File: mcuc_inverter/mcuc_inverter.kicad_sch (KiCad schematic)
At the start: 0 parts

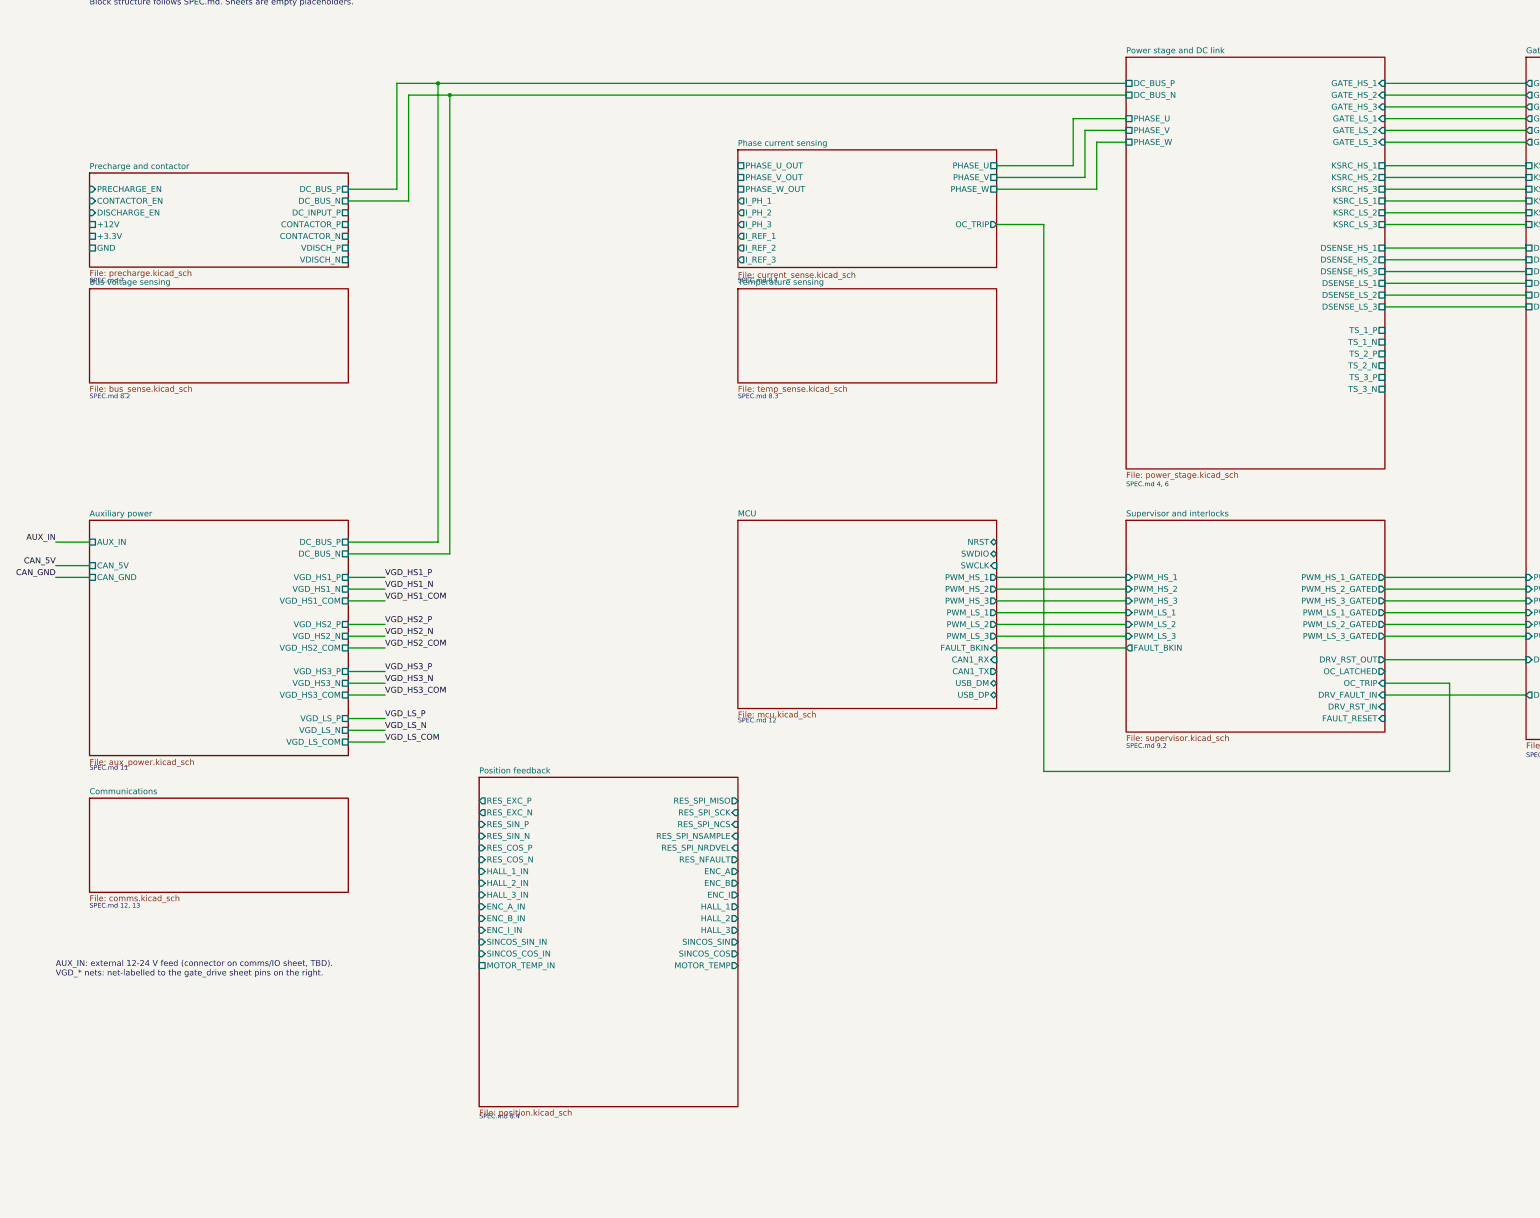
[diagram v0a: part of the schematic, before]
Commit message: Capture bus_sense, temp_sense, comms: all 11 sheets now live
bus_sense: 4x750k + 12.0k string (strict series, 124.5 V/part) into
AMC1311BDWV (pinout verified vs SBAS786C; B-grade 3.0-5.5 V VDD1 is
load-bearing per D022; no input clamp diodes per TI 9.3), HV-side
3.3 V from MCP1804T-3302 (2-28 V in, stocked - no TBV needed) off
the VGD_LS rail, diff-to-SE gain 0.75: V_BUS = 2.988 mV/V, 500 V ->
1.494 V, saturates ~1.50 V, always < 3.3 V.

temp_sense: coldplate NTC channel (B57861S off-board via J1101),
board NTC (NCU18 successor), 6x DNP TS provision pads onto the
module TS pins with D022 rationale quoted on-sheet.

comms: ISO1042DWR isolated CAN (VCC2 pins 11/16 tied - datasheet
requirement), split termination + TVS added (legacy sheet flagged
its own missing protection), USB-C + USBLC6 to MCU 70/71, keyed SWD,
status LEDs, I/O connectors. CAN_TX/RX verified onto MCU pins 96/95;
CONTACTOR_P/N resolve onto the precharge coil driver.

ERC 0 errors; netlist machine-checks per sheet; key cross-sheet
nets independently re-verified. 11 of 11 sheets captured.

Co-Authored-By: Claude Fable 5 <noreply@anthropic.com>
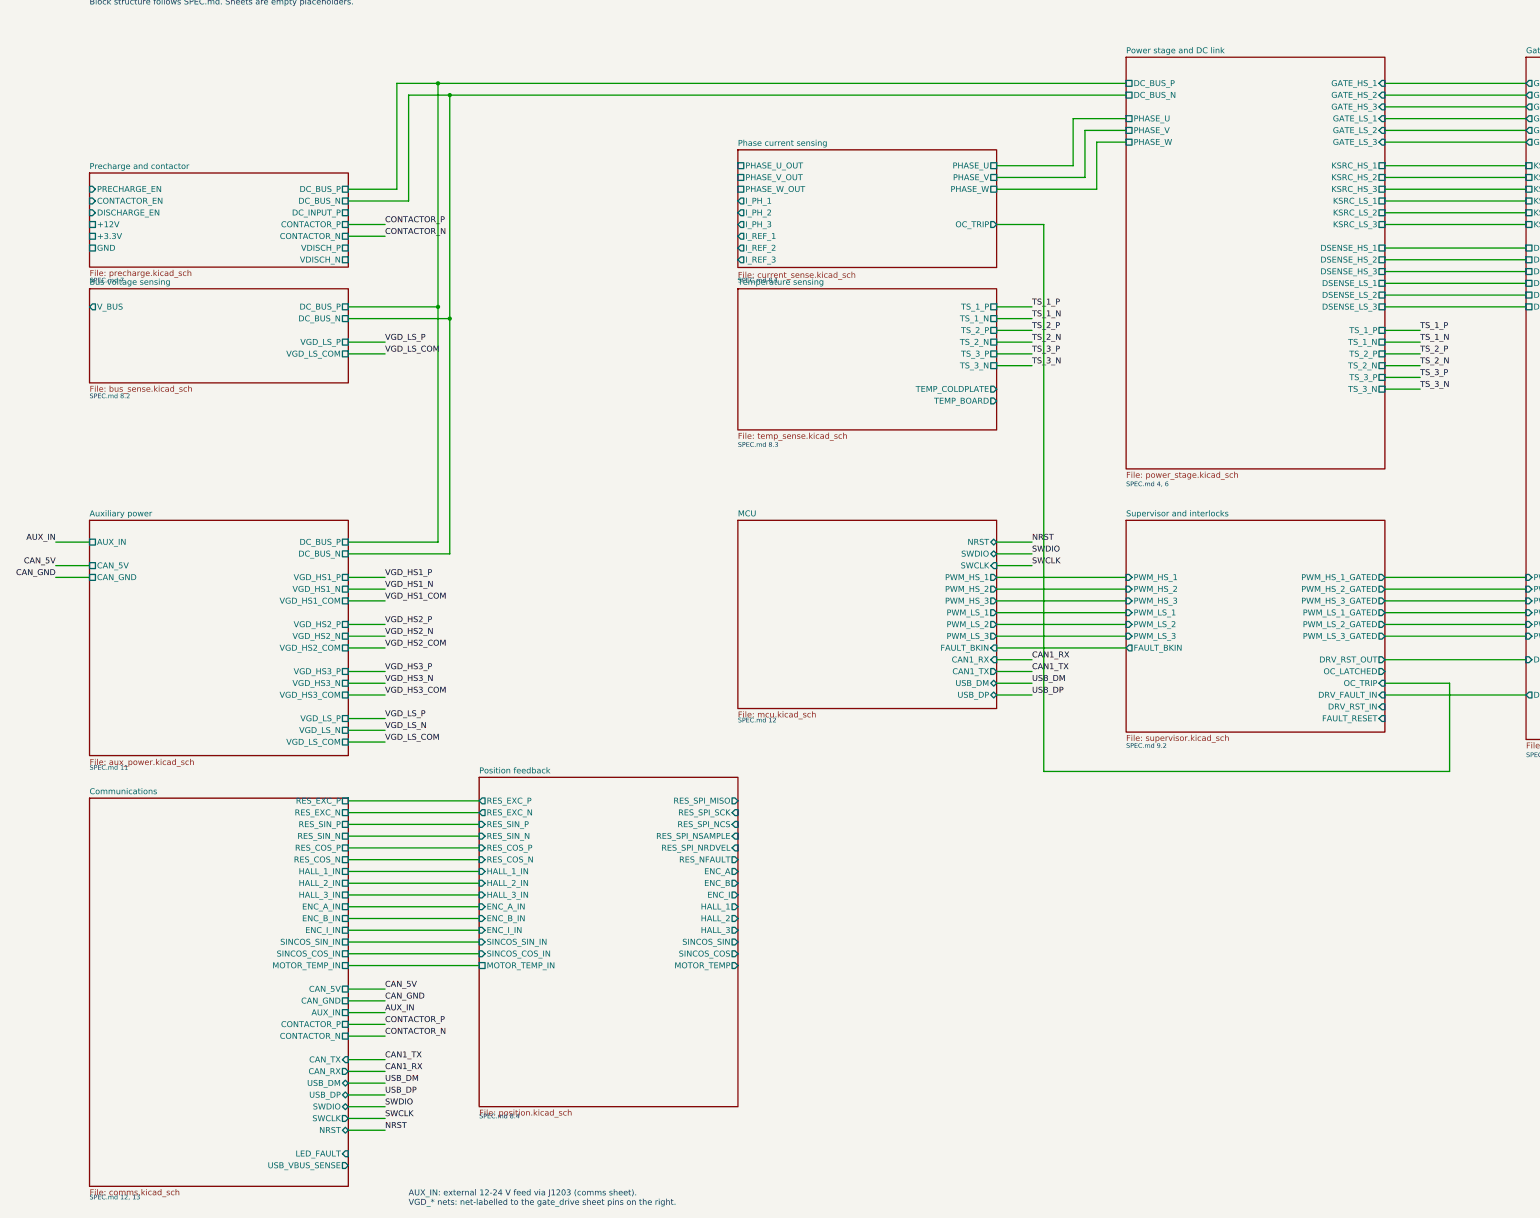
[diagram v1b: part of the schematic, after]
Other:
- sheet Bus voltage sensing ports: added DC_BUS_N, DC_BUS_P, VGD_LS_COM, VGD_LS_P, V_BUS; removed none
- sheet Communications ports: added AUX_IN, CAN_5V, CAN_GND, CAN_RX, CAN_TX, CONTACTOR_N, CONTACTOR_P, ENC_A_IN, ENC_B_IN, ENC_I_IN, HALL_1_IN, HALL_2_IN, HALL_3_IN, LED_FAULT, MOTOR_TEMP_IN, NRST, RES_COS_N, RES_COS_P, RES_EXC_N, RES_EXC_P, RES_SIN_N, RES_SIN_P, SINCOS_COS_IN, SINCOS_SIN_IN, SWCLK, SWDIO, USB_DM, USB_DP, USB_VBUS_SENSE; removed none
- sheet Temperature sensing ports: added TEMP_BOARD, TEMP_COLDPLATE, TS_1_N, TS_1_P, TS_2_N, TS_2_P, TS_3_N, TS_3_P; removed none
- note added: "AUX_IN: external 12-24 V feed via J1203 (comms sheet). VGD_* nets: net-labelled to the gate_drive sheet pins on the right."
- note removed: "AUX_IN: external 12-24 V feed (connector on comms/IO sheet, TBD). VGD_* nets: net-labelled to the gate_drive sheet pins on the right."

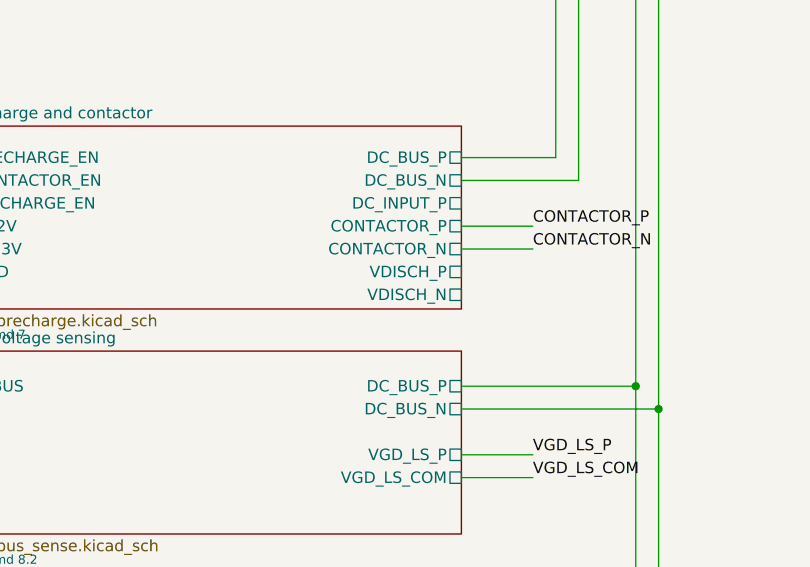
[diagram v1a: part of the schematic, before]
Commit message: Precharge: VOM1271T photovoltaic discharge drive; fix gate pulldown
Swap the active-discharge opto to VOM1271T (pinout verified from
Vishay 83469 Rev 1.9; SOP-4 symbol added to project lib) driven at
~19 mA from DISCHARGE_EN (R427 330R -> 100R). Deletes the
VDISCH_P/N floating-supply labels, flags and root pins entirely -
the photovoltaic driver needs no secondary supply and integrates
rapid gate turn-off.

Fix found during the swap: the 10k gate pulldown (R426) would have
clamped the VOM1271's 15-47 uA output to ~0.2 V - below the FET
threshold, discharge would never fire. Raised to 10M per the Vishay
test circuit; turn-off is handled by the driver's integrated
circuit, and the 10M still bleeds the gate if the driver is
unpopulated. Zener updated to stocked MM3Z18VT1G (D022 BOM sweep).

ERC 0 errors; netlist checks by the edit agent (LED loop, gate net,
DC_BUS_N membership, zero VDISCH nets remain).

Co-Authored-By: Claude Fable 5 <noreply@anthropic.com>
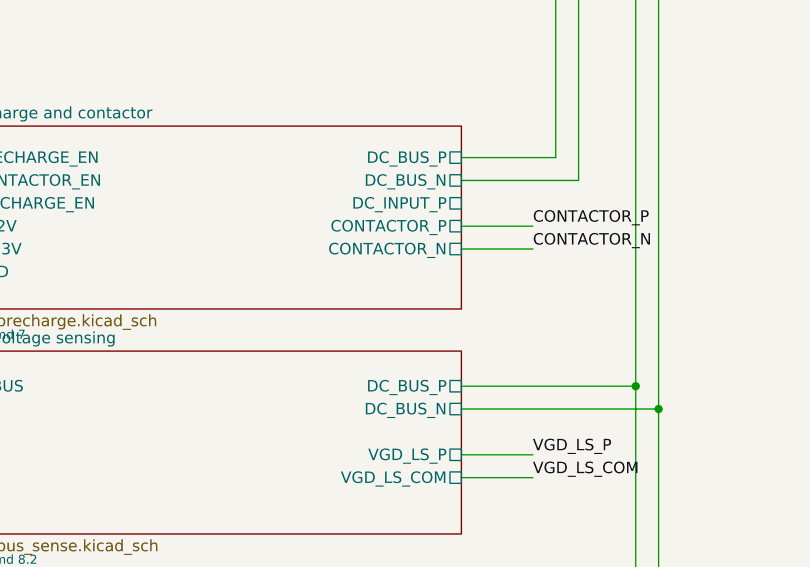
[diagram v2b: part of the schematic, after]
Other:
- sheet Precharge and contactor ports: added none; removed VDISCH_N, VDISCH_P
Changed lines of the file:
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@@
-			)
-		)
-		(pin "VDISCH_P" passive
-			(at 75.88 76.2 0)
-			(effects
-				(font
-					(size 1.27 1.27)
-				)
-				(justify right)
-			)
-		)
-		(pin "VDISCH_N" passive
-			(at 75.88 78.74 0)
-			(effects
-				(font
-					(size 1.27 1.27)
-				)
-				(justify right)
 			)
 		)

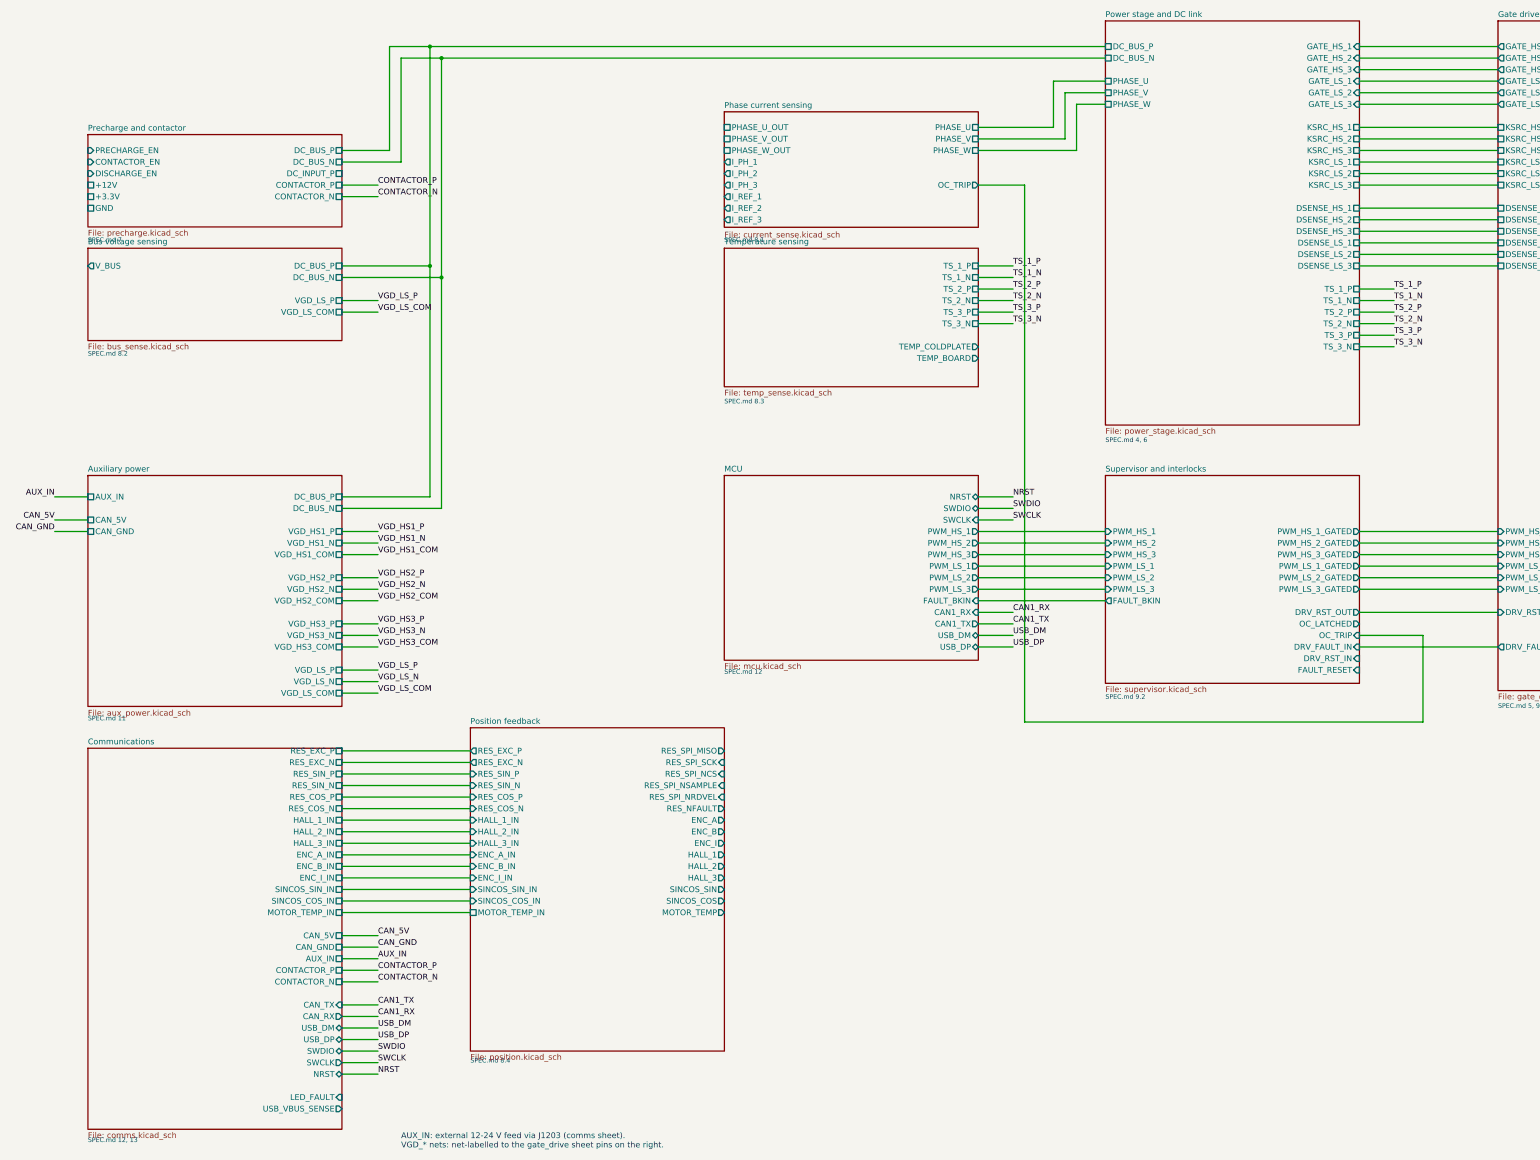
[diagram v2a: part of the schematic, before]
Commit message: Wire full MCU pin map; add verified PINOUT.md
All 33 remaining signals wired per the citation-verified map (D023):
phase currents PC0/1/2 on VESC triple-simultaneous ADC channels,
V_BUS PC3, temps PA3/PB0/PC4, SinCos PA5/PA6, I_REF PA4/PA7/PB1,
encoder PC6/7/8 (TIM3), halls PD12/13/14, resolver SPI3 PC10/PC11 +
PA15 boot-safe CS + PD0/PD1/PD2 controls, supervisor GPIOs PD3/4/5,
precharge/contactor/discharge PE2/3/4, LED PE0, VBUS sense PC5, PPM
PB6 (TIM4_CH1, VESC convention - repurposed J1206 spare pin).
PA0/1/2 and PB10/11 reserved with on-sheet notes.

AD2S1205 drive validated in-datasheet: VIH 2.0 V @ 5 V supply, so
3.3 V MCU outputs are legal; its 5 V outputs land on FT pins only.

docs/PINOUT.md: complete table with per-row DS8626 Table 7/9
citations, 5V-tolerance column with the analog-mode caveat, and the
D023 reservations - generated against the post-wiring netlist.

ERC 0 errors (warnings down 224 -> 201 as dangling pins connected).
33/33 nets machine-verified U1-pad-to-counterpart; 6 re-verified
independently before commit.

Co-Authored-By: Claude Fable 5 <noreply@anthropic.com>
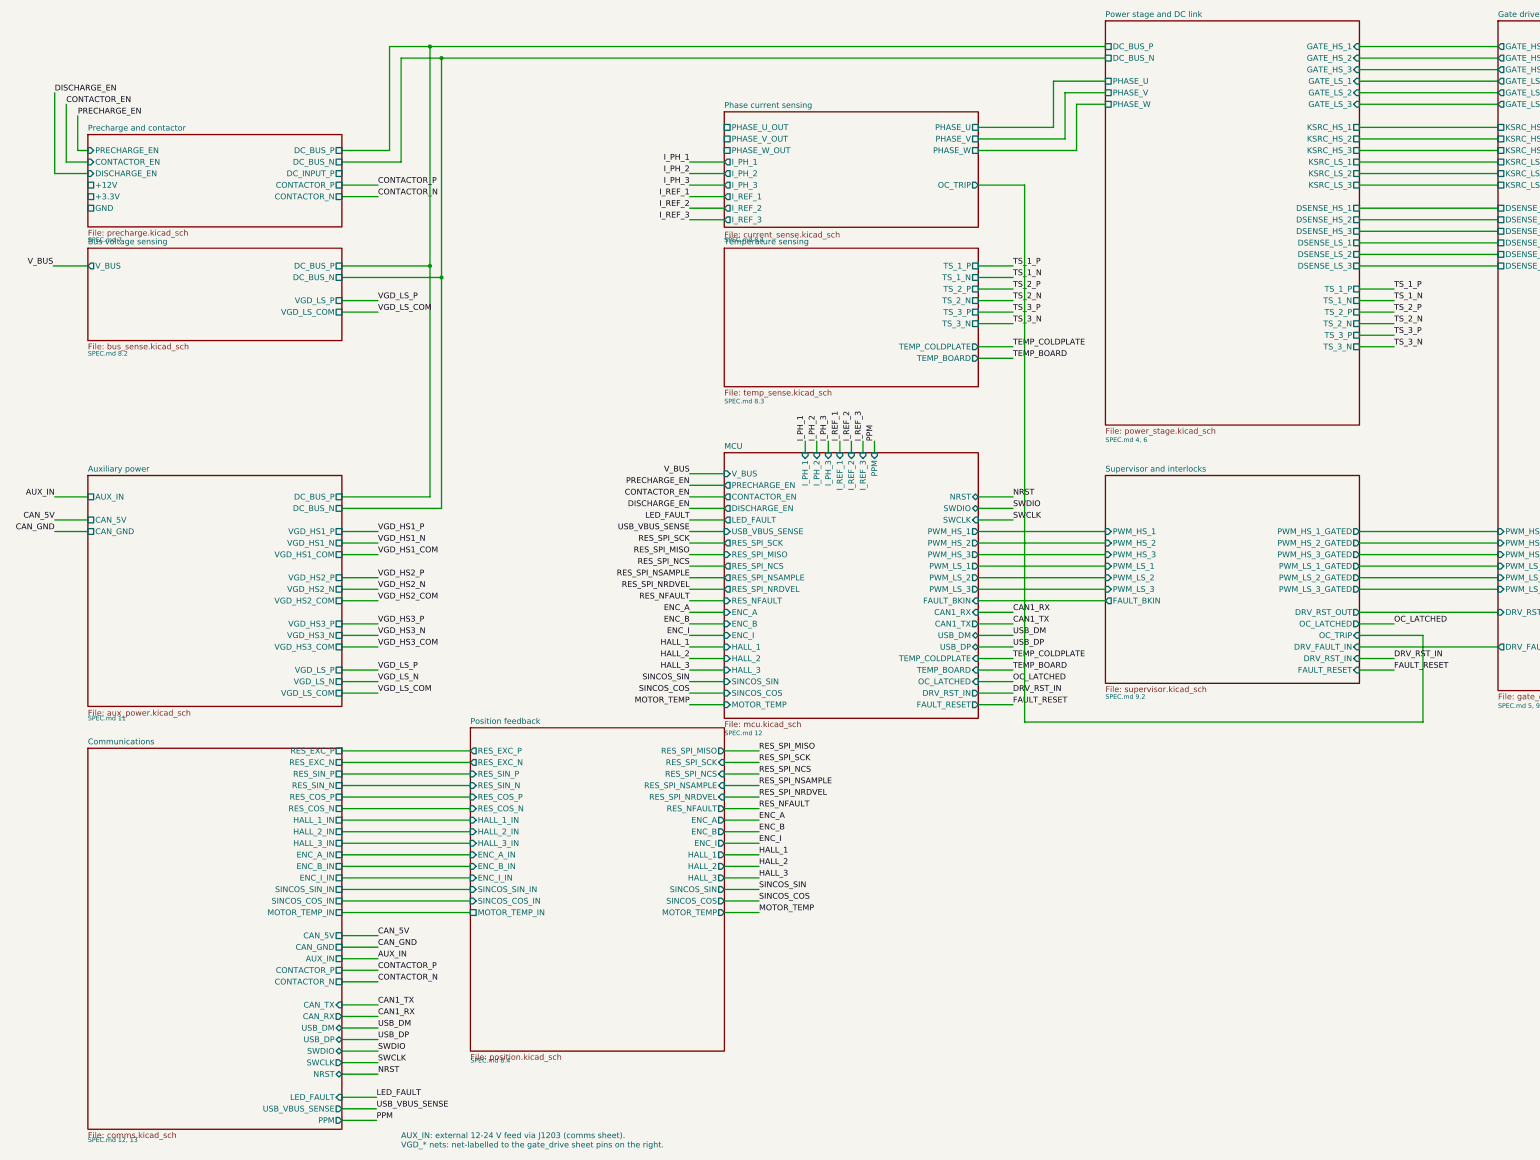
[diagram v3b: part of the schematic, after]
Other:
- sheet Communications ports: added PPM; removed none
- sheet MCU ports: added CONTACTOR_EN, DISCHARGE_EN, DRV_RST_IN, ENC_A, ENC_B, ENC_I, FAULT_RESET, HALL_1, HALL_2, HALL_3, I_PH_1, I_PH_2, I_PH_3, I_REF_1, I_REF_2, I_REF_3, LED_FAULT, MOTOR_TEMP, OC_LATCHED, PPM, PRECHARGE_EN, RES_NFAULT, RES_SPI_MISO, RES_SPI_NCS, RES_SPI_NRDVEL, RES_SPI_NSAMPLE, RES_SPI_SCK, SINCOS_COS, SINCOS_SIN, TEMP_BOARD, TEMP_COLDPLATE, USB_VBUS_SENSE, V_BUS; removed none
